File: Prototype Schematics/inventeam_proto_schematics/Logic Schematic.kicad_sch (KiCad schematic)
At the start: 44 parts, among them J2001 Conn_02x20_Top_Bottom, J2002 Conn_01x03, J2003 Screw_Terminal_01x02, U2001 MCP23S17_SP, U2002 TMUX1208PW, U2003 MCP23S17_SP, U2004 TMUX1208PW, U2005 MCP1525-TO, U2006 OPA2333xxD

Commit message: V17
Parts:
- renumbered C2009 to C2007, C2007 to C2009, U2006 to U2005, U2005 to U2006

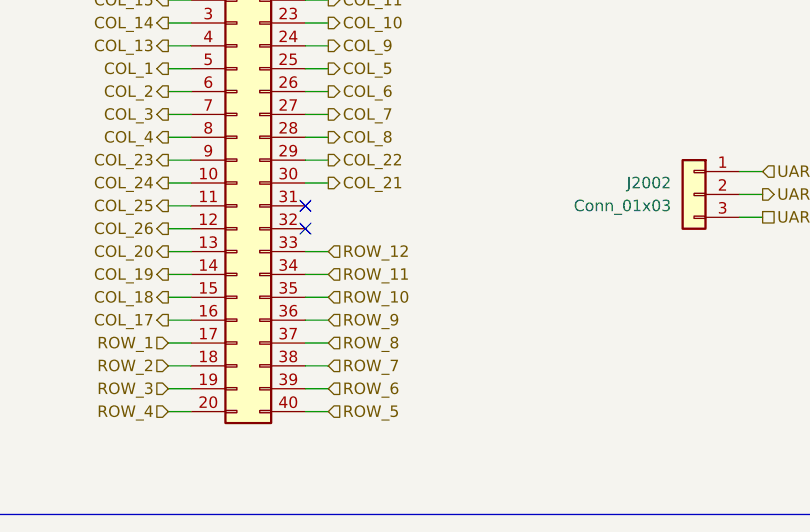
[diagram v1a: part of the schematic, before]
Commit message: Ground header pin for thermistor pcb
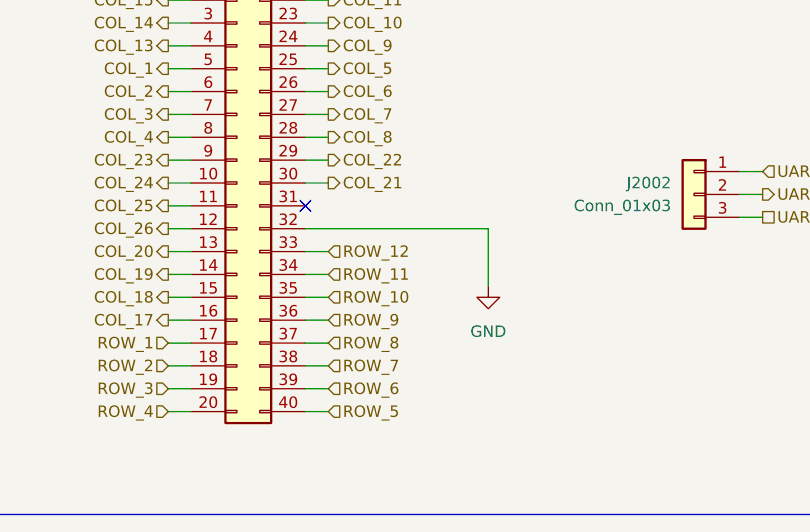
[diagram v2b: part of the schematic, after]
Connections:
- net GND: now also J2001.32 (Pin_32)
- no-connect marks 24 -> 23
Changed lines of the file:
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@@
 		(at 304.8 177.8)
 	)
-	(no_connect
-		(at 83.82 332.74)
-	)
 	(wire
 		(pts
@@
 	(wire
 		(pts
+			(xy 104.14 332.74) (xy 104.14 339.09)
+		)
+		(stroke
+			(width 0)
+			(type default)
+		)
+	)
+	(wire
+		(pts
 			(xy 161.29 114.3) (xy 161.29 116.84)
 		)
@@
 	(wire
 		(pts
+			(xy 83.82 332.74) (xy 104.14 332.74)
+		)
+		(stroke
+			(width 0)
+			(type default)
+		)
+	)
+	(wire
+		(pts
 			(xy 68.58 327.66) (xy 71.12 327.66)
 		)
@@
 					(unit 1)
 				)
+			)
+		)
+	)
+	(symbol
+		(lib_id "power:GND")
+		(at 104.14 339.09 0)
+		(unit 1)
+		(exclude_from_sim no)
+		(in_bom yes)
+		(on_board yes)
+		(dnp no)
+		(fields_autoplaced yes)
+		(property "Reference" "#PWR01"
+			(at 104.14 345.44 0)
+			(effects
+				(font
+					(size 1.27 1.27)
+				)
+				(hide yes)
+			)
+		)
+		(property "Value" "GND"
+			(at 104.14 344.17 0)
+			(effects
+				(font
+					(size 1.27 1.27)
+				)
+			)
+		)
+		(property "Footprint" ""
+			(at 104.14 339.09 0)
+			(effects
+				(font
+					(size 1.27 1.27)
+				)
+				(hide yes)
+			)
+		)
+		(property "Datasheet" ""
+			(at 104.14 339.09 0)
+			(effects
+				(font
+					(size 1.27 1.27)
+				)
+				(hide yes)
+			)
+		)
+		(property "Description" "Power symbol creates a global label with name \"GND\" , ground"
+			(at 104.14 339.09 0)
+			(effects
+				(font
+					(size 1.27 1.27)
+				)
+				(hide yes)
+			)
+		)
+		(pin "1"
+		)
+		(instances
+			(project ""
+				(path "/b2b47a1d-b0e5-4b64-b5c3-0417d2d1887a/9f4817f9-c513-4659-982a-bb656752ed3c"
+					(reference "#PWR01")
+					(unit 1)
+				)
+				(path "/b2b47a1d-b0e5-4b64-b5c3-0417d2d1887a/cce3bfa4-7555-4887-9571-c1a2b294f16b"
+					(reference "#PWR02")
+					(unit 1)
+				)
